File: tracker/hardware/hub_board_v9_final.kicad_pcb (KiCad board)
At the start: 4 copper layers, 103 x 103 mm, 39 parts, among them U1 ESP32-S3-WROOM-1U-N8R8, U2 LoRa2021F33-2G4, U3 LoRa2021_Castellated, U4 SX1280, U5 MAX-M10S, U6 MS5611-01BA, U7 TPS7A02

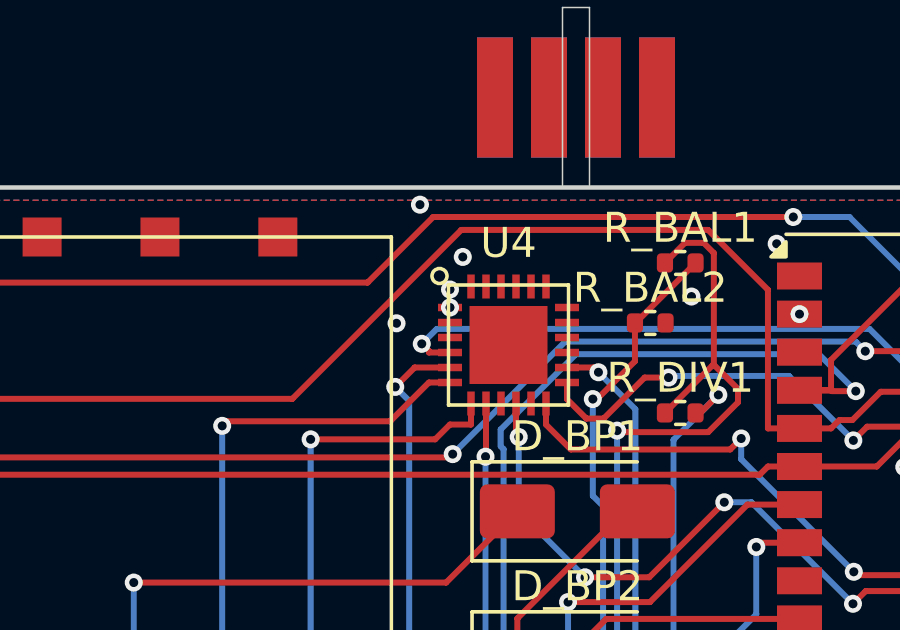
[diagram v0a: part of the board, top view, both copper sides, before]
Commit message: fix(pcb): stub the moved via back to U4 pad 2 -- 34/21 restored
Moving the +3V3 vias clear of U4 GND pad 3 broke their own connection to U4
pad 2 [+3V3]. Add a 0.5 mm F.Cu stub on the same net. Same-net only; refuses
foreign nets. unconnected 22 -> 21.

Current best: 34 violations / 21 unconnected (from 44/23 at baseline).
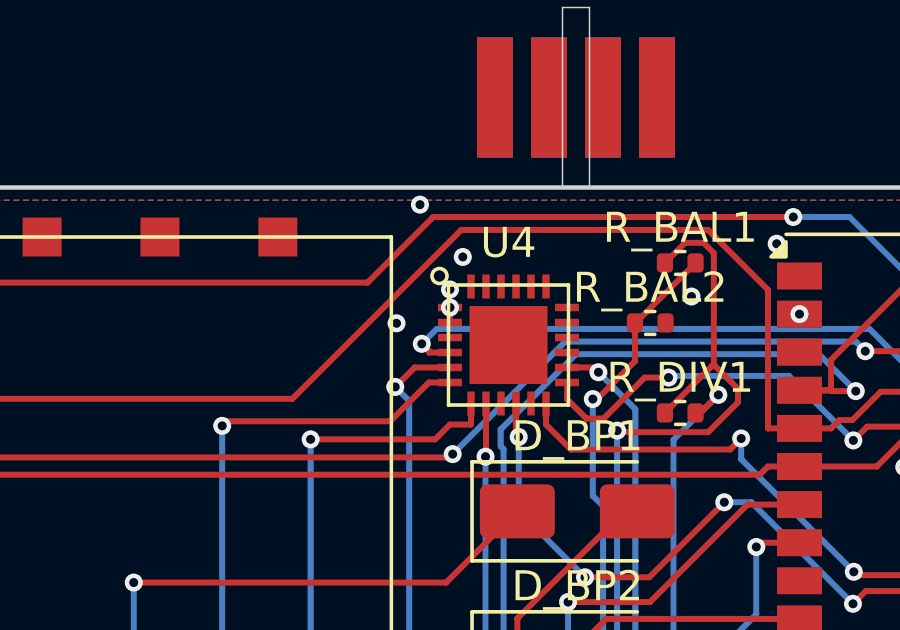
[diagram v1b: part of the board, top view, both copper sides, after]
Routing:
- net +3V3: track 0.00 -> 0.50 mm
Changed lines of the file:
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@@
 		(layer "Edge.Cuts")
+	)
+	(segment
+		(start 47.3 4.5)
+		(end 47.3 4)
+		(width 0.2)
+		(layer "F.Cu")
+		(net 1)
 	)
 	(via blind
